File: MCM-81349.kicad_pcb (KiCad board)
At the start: 2 copper layers, 65 x 65 mm, 168 parts, among them J1 Conn_01x04, J10 JACK-L-LKWGPC-5A(R), J11 Conn_02x02_Odd_Even, J2 /, J5 USB4105-GF-A, J7 Conn_01x04, J9 /, Q1 BUK9K61-100LX, Q2 BUK9K61-100LX, Q3 BUK9K61-100LX, Q8 BC846BLT1G, U1 AZ1117CR-3.3TRG1, U2 LMR16006YDDCR, U3 TMUX1219DCKR, U4 MLX81349-KLW-AMX-000, U5 ESP32-S3-WROOM-1-N16R8, U6 TXS0102DCTT, U7 BTH50060-1LUA, U8 BUK7Y38-100E

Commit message: generate v1.1 data
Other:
- board text added: "MCM 81349 v1.1"
- board text removed: "MCM 81349 v1.0"

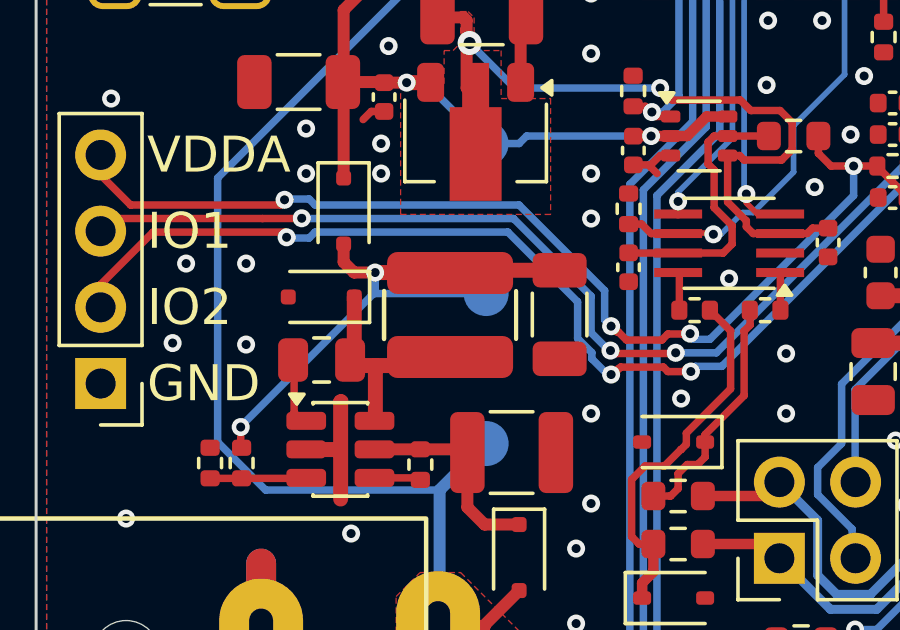
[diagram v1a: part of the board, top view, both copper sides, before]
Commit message: replace coil with digikey available version
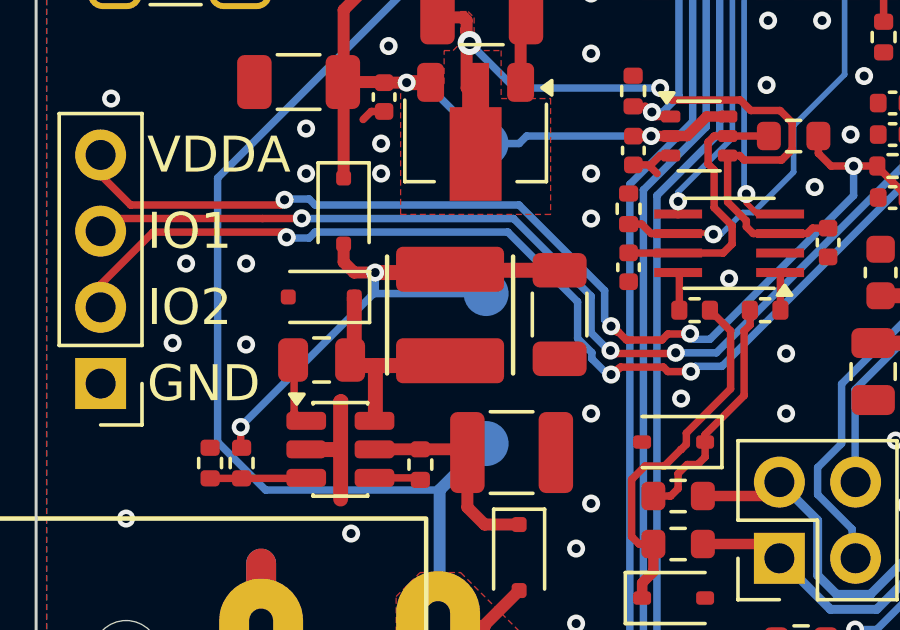
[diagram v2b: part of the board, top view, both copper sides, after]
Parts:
- L1: value 6.8uH -> 47uH; footprint extra:HPC4018NF-Series -> Extra:WE-LQS
- R22, R24: value TBD -> 9k53
- R23, R25: value TBD -> 430R
- R4: value 54k9 -> 39k
- R5: value 10k -> 6k2
- U2: value LMR16006YDDCR -> LV2862XLVDDCR

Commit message: coderabbitai review comments
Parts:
- L1: footprint Extra:WE-LQS -> extra:WE-LQS
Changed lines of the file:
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@@
 			)
 		)
-		(property "Description" "RES 57.6K OHM 1% 1/16W 0402"
+		(property "Description" "RES 39K OHM 1% 1/16W 0402"
 			(at 0 0 90)
 			(layer "F.Fab")
@@
 			)
 		)
-		(property "Description" "RES SMD 10K5 OHM 1% 1/16W 0402"
+		(property "Description" "RES SMD 6K2 OHM 1% 1/16W 0402"
 			(at 0 0 90)
 			(layer "F.Fab")
@@
 		)
 	)
-	(footprint "Extra:WE-LQS"
+	(footprint "extra:WE-LQS"
 		(layer "F.Cu")
 		(at 73.7986 75.7152 90)
